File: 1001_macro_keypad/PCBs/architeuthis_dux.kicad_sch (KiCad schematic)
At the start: 32 parts, among them J1 ePaperModule, J2 RotaryModule_01, J3 RotaryModule_02, SW01 MX_SW, SW10 MX_SW, SW11 MX_SW, SW12 MX_SW, SW13 MX_SW, SW14 MX_SW, SW2 MX_SW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

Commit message: epaper 테스트
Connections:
- net +5V: no longer J1.1 (BUSY)
- net VSYS: now reaches U1.39 (VSYS)
- net VSYS: now also J1.1 (BUSY)
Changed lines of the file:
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@@
+    )
+  )
+  (global_label "VSYS" (shape input) (at 208.28 77.47 180) (fields_autoplaced)
+    (effects (font (size 1.27 1.27)) (justify right))
+    (property "Intersheetrefs" "${INTERSHEET_REFS}" (at 200.778 77.47 0)
+      (effects (font (size 1.27 1.27)) (justify right) hide)
     )
   )
@@
     (effects (font (size 1.27 1.27)) (justify left))
     (property "Intersheetrefs" "${INTERSHEET_REFS}" (at 99.6072 49.53 0)
+      (effects (font (size 1.27 1.27)) (justify left) hide)
+    )
+  )
+  (global_label "VSYS" (shape input) (at 151.13 44.45 0) (fields_autoplaced)
+    (effects (font (size 1.27 1.27)) (justify left))
+    (property "Intersheetrefs" "${INTERSHEET_REFS}" (at 158.632 44.45 0)
       (effects (font (size 1.27 1.27)) (justify left) hide)
     )
@@
         )
       )
-    )
-  )
-  (symbol (lib_id "power:+5V") (at 208.28 77.47 90) (unit 1)
-    (in_bom yes) (on_board yes) (dnp no) (fields_autoplaced)
-    (property "Reference" "#PWR02" (at 212.09 77.47 0)
-      (effects (font (size 1.27 1.27)) hide)
-    )
-    (property "Value" "+5V" (at 204.47 78.105 90)
-      (effects (font (size 1.27 1.27)) (justify left))
-    )
-    (property "Footprint" "" (at 208.28 77.47 0)
-      (effects (font (size 1.27 1.27)) hide)
-    )
-    (property "Datasheet" "" (at 208.28 77.47 0)
-      (effects (font (size 1.27 1.27)) hide)
-    )
-    (pin "1")
-    (instances
-      (project "architeuthis_dux"
-        (path "/4d2fbfb9-c67d-4ccb-bbaa-2d2f4be0cbd8"
-          (reference "#PWR02") (unit 1)
-        )
-      )

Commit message: 배선 변경 및 라이브러리 추가
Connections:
- net at J2.2 (KEY): no longer U1.25 (GPIO19)
- net at J2.3 (S2): no longer U1.24 (GPIO18)
- net at J2.4 (S1): no longer U1.22 (GPIO17)
- net at J3.2 (Pin_2): no longer U1.21 (GPIO16)
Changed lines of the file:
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@@
-    (stroke (width 0) (type default))
-  )
-  (wire (pts (xy 161.29 109.22) (xy 176.53 109.22))
     (stroke (width 0) (type default))
   )
@@
     (stroke (width 0) (type default))
   )
-  (wire (pts (xy 161.29 90.17) (xy 161.29 109.22))
-    (stroke (width 0) (type default))
-  )
   (wire (pts (xy 48.26 99.06) (xy 60.96 99.06))
     (stroke (width 0) (type default))
   )
-  (wire (pts (xy 151.13 80.01) (xy 167.64 80.01))
-    (stroke (width 0) (type default))
-  )
   (wire (pts (xy 115.57 90.17) (xy 115.57 114.3))
-    (stroke (width 0) (type default))
-  )
-  (wire (pts (xy 167.64 93.98) (xy 176.53 93.98))
-    (stroke (width 0) (type default))
-  )
-  (wire (pts (xy 167.64 80.01) (xy 167.64 93.98))
     (stroke (width 0) (type default))
   )
@@
     (stroke (width 0) (type default))
   )
-  (wire (pts (xy 163.83 87.63) (xy 163.83 99.06))
-    (stroke (width 0) (type default))
-  )
   (wire (pts (xy 151.13 74.93) (xy 191.77 74.93))
     (stroke (width 0) (type default))
   )
   (wire (pts (xy 53.34 96.52) (xy 38.1 96.52))
-    (stroke (width 0) (type default))
-  )
-  (wire (pts (xy 165.1 96.52) (xy 176.53 96.52))
     (stroke (width 0) (type default))
   )
@@
     (stroke (width 0) (type default))
   )
-  (wire (pts (xy 163.83 99.06) (xy 176.53 99.06))
-    (stroke (width 0) (type default))
-  )
   (wire (pts (xy 66.04 93.98) (xy 53.34 93.98))
-    (stroke (width 0) (type default))
-  )
-  (wire (pts (xy 151.13 82.55) (xy 165.1 82.55))
     (stroke (width 0) (type default))
   )
@@
     (stroke (width 0) (type default))
   )
-  (wire (pts (xy 151.13 90.17) (xy 161.29 90.17))
-    (stroke (width 0) (type default))
-  )
   (wire (pts (xy 189.23 77.47) (xy 151.13 77.47))
     (stroke (width 0) (type default))
   )
   (wire (pts (xy 81.28 66.04) (xy 91.44 66.04))
-    (stroke (width 0) (type default))
-  )
-  (wire (pts (xy 151.13 87.63) (xy 163.83 87.63))
     (stroke (width 0) (type default))
   )
@@
     (stroke (width 0) (type default))
   )
-  (wire (pts (xy 165.1 82.55) (xy 165.1 96.52))
-    (stroke (width 0) (type default))
-  )

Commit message: 설계 픽스 및 모델링 작업 시작
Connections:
- net at J1.3 (D/C): now also U1.25 (GPIO19); no longer U1.34 (GPIO28_ADC2)
- net at J1.4 (CS): now also U1.24 (GPIO18); no longer U1.26 (GPIO20)
- net at J1.5 (SCL): now also U1.26 (GPIO20); no longer U1.32 (GPIO27_ADC1)
- net at J1.6 (SDA): now also U1.21 (GPIO16); no longer U1.27 (GPIO21)
- net at J1.7 (GND): now also U1.22 (GPIO17); no longer U1.31 (GPIO26_ADC0)
- net at J1.8 (VCC): now also U1.27 (GPIO21); no longer U1.29 (GPIO22)
- net at J2.2 (KEY): now also U1.11 (GPIO8)
- net at J2.3 (S2): now also U1.12 (GPIO9)
- net at J2.4 (S1): now also U1.14 (GPIO10)
- net at J3.2 (Pin_2): now also U1.17 (GPIO13)
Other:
- moved on the sheet: J1
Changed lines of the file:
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@@
   (junction (at 81.28 49.53) (diameter 0) (color 0 0 0 0)
   )
-  (wire (pts (xy 199.39 87.63) (xy 208.28 87.63))
-    (stroke (width 0) (type default))
-  )
   (wire (pts (xy 45.72 111.76) (xy 45.72 125.73))
     (stroke (width 0) (type default))
   )
-  (wire (pts (xy 200.66 57.15) (xy 151.13 57.15))
+  (wire (pts (xy 171.45 77.47) (xy 171.45 64.77))
     (stroke (width 0) (type default))
   )
@@
     (stroke (width 0) (type default))
   )
+  (wire (pts (xy 151.13 90.17) (xy 168.91 90.17))
+    (stroke (width 0) (type default))
+  )
   (wire (pts (xy 38.1 111.76) (xy 45.72 111.76))
     (stroke (width 0) (type default))
   )
-  (wire (pts (xy 189.23 85.09) (xy 189.23 77.47))
-    (stroke (width 0) (type default))
-  )
-  (wire (pts (xy 208.28 95.25) (xy 194.31 95.25))
-    (stroke (width 0) (type default))
-  )
-  (wire (pts (xy 199.39 62.23) (xy 199.39 87.63))
-    (stroke (width 0) (type default))
-  )
-  (wire (pts (xy 113.03 111.76) (xy 113.03 87.63))
-    (stroke (width 0) (type default))
-  )
   (wire (pts (xy 48.26 49.53) (xy 64.77 49.53))
     (stroke (width 0) (type default))
   )
+  (wire (pts (xy 151.13 82.55) (xy 167.64 82.55))
+    (stroke (width 0) (type default))
+  )
+  (wire (pts (xy 115.57 90.17) (xy 101.6 90.17))
+    (stroke (width 0) (type default))
+  )
+  (wire (pts (xy 101.6 90.17) (xy 101.6 114.3))
+    (stroke (width 0) (type default))
+  )
   (wire (pts (xy 33.02 99.06) (xy 48.26 99.06))
     (stroke (width 0) (type default))
   )
-  (wire (pts (xy 176.53 111.76) (xy 113.03 111.76))
-    (stroke (width 0) (type default))
-  )
   (wire (pts (xy 64.77 66.04) (xy 81.28 66.04))
     (stroke (width 0) (type default))
   )
+  (wire (pts (xy 176.53 93.98) (xy 109.22 93.98))
+    (stroke (width 0) (type default))
+  )
   (wire (pts (xy 48.26 99.06) (xy 60.96 99.06))
     (stroke (width 0) (type default))
   )
-  (wire (pts (xy 115.57 90.17) (xy 115.57 114.3))
+  (wire (pts (xy 104.14 74.93) (xy 104.14 99.06))
     (stroke (width 0) (type default))
   )
@@
     (stroke (width 0) (type default))
   )
-  (wire (pts (xy 208.28 92.71) (xy 196.85 92.71))
-    (stroke (width 0) (type default))
-  )
-  (wire (pts (xy 208.28 82.55) (xy 200.66 82.55))
-    (stroke (width 0) (type default))
-  )
-  (wire (pts (xy 200.66 82.55) (xy 200.66 57.15))
-    (stroke (width 0) (type default))
-  )
-  (wire (pts (xy 113.03 87.63) (xy 115.57 87.63))
-    (stroke (width 0) (type default))
-  )
   (wire (pts (xy 38.1 111.76) (xy 38.1 115.57))
     (stroke (width 0) (type default))
   )
-  (wire (pts (xy 151.13 62.23) (xy 199.39 62.23))
-    (stroke (width 0) (type default))
-  )
   (wire (pts (xy 53.34 111.76) (xy 53.34 115.57))
     (stroke (width 0) (type default))
   )
-  (wire (pts (xy 151.13 74.93) (xy 191.77 74.93))
+  (wire (pts (xy 165.1 59.69) (xy 177.8 59.69))
+    (stroke (width 0) (type default))
+  )
+  (wire (pts (xy 173.99 69.85) (xy 177.8 69.85))
+    (stroke (width 0) (type default))
+  )
+  (wire (pts (xy 168.91 67.31) (xy 177.8 67.31))
+    (stroke (width 0) (type default))
+  )
+  (wire (pts (xy 176.53 114.3) (xy 101.6 114.3))
     (stroke (width 0) (type default))
   )
@@
     (stroke (width 0) (type default))
   )
+  (wire (pts (xy 151.13 80.01) (xy 165.1 80.01))
+    (stroke (width 0) (type default))
+  )
   (wire (pts (xy 38.1 93.98) (xy 38.1 96.52))
     (stroke (width 0) (type default))
   )
+  (wire (pts (xy 106.68 96.52) (xy 106.68 69.85))
+    (stroke (width 0) (type default))
+  )
+  (wire (pts (xy 110.49 87.63) (xy 115.57 87.63))
+    (stroke (width 0) (type default))
+  )
   (wire (pts (xy 66.04 125.73) (xy 66.04 93.98))
     (stroke (width 0) (type default))
@@
     (stroke (width 0) (type default))
   )
+  (wire (pts (xy 109.22 67.31) (xy 109.22 93.98))
+    (stroke (width 0) (type default))
+  )
   (wire (pts (xy 53.34 111.76) (xy 53.34 96.52))
     (stroke (width 0) (type default))
   )
+  (wire (pts (xy 167.64 82.55) (xy 167.64 62.23))
+    (stroke (width 0) (type default))
+  )
+  (wire (pts (xy 106.68 69.85) (xy 115.57 69.85))
+    (stroke (width 0) (type default))
+  )
   (wire (pts (xy 66.04 93.98) (xy 53.34 93.98))
     (stroke (width 0) (type default))
@@
     (stroke (width 0) (type default))
   )
-  (wire (pts (xy 115.57 114.3) (xy 176.53 114.3))
-    (stroke (width 0) (type default))
-  )
-  (wire (pts (xy 191.77 74.93) (xy 191.77 90.17))
+  (wire (pts (xy 113.03 82.55) (xy 113.03 109.22))
+    (stroke (width 0) (type default))
+  )
+  (wire (pts (xy 104.14 74.93) (xy 115.57 74.93))
+    (stroke (width 0) (type default))
+  )
+  (wire (pts (xy 151.13 74.93) (xy 177.8 74.93))
+    (stroke (width 0) (type default))
+  )
+  (wire (pts (xy 151.13 87.63) (xy 173.99 87.63))
+    (stroke (width 0) (type default))
+  )
+  (wire (pts (xy 168.91 90.17) (xy 168.91 67.31))
     (stroke (width 0) (type default))
   )
@@
     (stroke (width 0) (type default))
   )
-  (wire (pts (xy 194.31 69.85) (xy 151.13 69.85))
-    (stroke (width 0) (type default))
-  )
-  (wire (pts (xy 194.31 95.25) (xy 194.31 69.85))
+  (wire (pts (xy 176.53 109.22) (xy 113.03 109.22))
     (stroke (width 0) (type default))
   )
@@
     (stroke (width 0) (type default))
   )
-  (wire (pts (xy 208.28 85.09) (xy 189.23 85.09))
-    (stroke (width 0) (type default))
-  )
   (wire (pts (xy 86.36 93.98) (xy 86.36 78.74))
     (stroke (width 0) (type default))
   )
-  (wire (pts (xy 191.77 90.17) (xy 208.28 90.17))
-    (stroke (width 0) (type default))
-  )
-  (wire (pts (xy 196.85 92.71) (xy 196.85 64.77))
+  (wire (pts (xy 109.22 67.31) (xy 115.57 67.31))
+    (stroke (width 0) (type default))
+  )
+  (wire (pts (xy 113.03 82.55) (xy 115.57 82.55))
     (stroke (width 0) (type default))
   )
@@
     (stroke (width 0) (type default))
   )
+  (wire (pts (xy 165.1 80.01) (xy 165.1 59.69))
+    (stroke (width 0) (type default))
+  )
+  (wire (pts (xy 173.99 87.63) (xy 173.99 69.85))
+    (stroke (width 0) (type default))
+  )
   (wire (pts (xy 48.26 81.28) (xy 64.77 81.28))
     (stroke (width 0) (type default))
@@
     (stroke (width 0) (type default))
   )
-  (wire (pts (xy 196.85 64.77) (xy 151.13 64.77))
-    (stroke (width 0) (type default))
-  )
-  (wire (pts (xy 189.23 77.47) (xy 151.13 77.47))
+  (wire (pts (xy 176.53 111.76) (xy 110.49 111.76))
+    (stroke (width 0) (type default))
+  )
+  (wire (pts (xy 167.64 62.23) (xy 177.8 62.23))
+    (stroke (width 0) (type default))
+  )
+  (wire (pts (xy 171.45 64.77) (xy 177.8 64.77))
+    (stroke (width 0) (type default))
+  )
+  (wire (pts (xy 177.8 74.93) (xy 177.8 72.39))
     (stroke (width 0) (type default))
   )
@@
     (stroke (width 0) (type default))
   )
+  (wire (pts (xy 110.49 111.76) (xy 110.49 87.63))
+    (stroke (width 0) (type default))
+  )
   (wire (pts (xy 33.02 66.04) (xy 48.26 66.04))
     (stroke (width 0) (type default))
   )
   (wire (pts (xy 38.1 78.74) (xy 38.1 93.98))
+    (stroke (width 0) (type default))
+  )
+  (wire (pts (xy 176.53 99.06) (xy 104.14 99.06))
+    (stroke (width 0) (type default))
+  )
+  (wire (pts (xy 176.53 96.52) (xy 106.68 96.52))
+    (stroke (width 0) (type default))
+  )
+  (wire (pts (xy 151.13 77.47) (xy 171.45 77.47))
     (stroke (width 0) (type default))
   )
@@
     )
   )
-  (global_label "VSYS" (shape input) (at 208.28 77.47 180) (fields_autoplaced)
-    (effects (font (size 1.27 1.27)) (justify right))
-    (property "Intersheetrefs" "${INTERSHEET_REFS}" (at 200.778 77.47 0)
+  (global_label "VSYS" (shape input) (at 177.8 54.61 180) (fields_autoplaced)
+    (effects (font (size 1.27 1.27)) (justify right))
+    (property "Intersheetrefs" "${INTERSHEET_REFS}" (at 170.298 54.61 0)
       (effects (font (size 1.27 1.27)) (justify right) hide)
     )
@@
     )
   )
-  (symbol (lib_id "Connector_Generic:Conn_01x08") (at 213.36 85.09 0) (unit 1)
-    (in_bom yes) (on_board yes) (dnp no) (fields_autoplaced)
-    (property "Reference" "J1" (at 215.9 85.725 0)
+  (symbol (lib_id "Connector_Generic:Conn_01x08") (at 182.88 62.23 0) (unit 1)
+    (in_bom yes) (on_board yes) (dnp no) (fields_autoplaced)
+    (property "Reference" "J1" (at 185.42 62.865 0)
       (effects (font (size 1.27 1.27)) (justify left))
     )
-    (property "Value" "ePaperModule" (at 215.9 88.265 0)
+    (property "Value" "ePaperModule" (at 185.42 65.405 0)
       (effects (font (size 1.27 1.27)) (justify left))
     )
-    (property "Footprint" "Connector_PinHeader_2.54mm:PinHeader_2x04_P2.54mm_Vertical" (at 213.36 85.09 0)
-      (effects (font (size 1.27 1.27)) hide)
-    )
-    (property "Datasheet" "~" (at 213.36 85.09 0)
+    (property "Footprint" "Connector_PinHeader_2.54mm:PinHeader_2x04_P2.54mm_Vertical" (at 182.88 62.23 0)
+      (effects (font (size 1.27 1.27)) hide)
+    )
+    (property "Datasheet" "~" (at 182.88 62.23 0)
       (effects (font (size 1.27 1.27)) hide)
     )
@@
     )
   )
-  (symbol (lib_id "power:GND") (at 208.28 80.01 270) (unit 1)
-    (in_bom yes) (on_board yes) (dnp no) (fields_autoplaced)
-    (property "Reference" "#PWR014" (at 201.93 80.01 0)
-      (effects (font (size 1.27 1.27)) hide)
-    )
-    (property "Value" "GND" (at 204.47 80.645 90)
-      (effects (font (size 1.27 1.27)) (justify right))
-    )
-    (property "Footprint" "" (at 208.28 80.01 0)
-      (effects (font (size 1.27 1.27)) hide)
-    )
-    (property "Datasheet" "" (at 208.28 80.01 0)
-      (effects (font (size 1.27 1.27)) hide)
-    )
+  (symbol (lib_id "power:GND") (at 177.8 57.15 270) (unit 1)
+    (in_bom yes) (on_board yes) (dnp no) (fields_autoplaced)
+    (property "Reference" "#PWR014" (at 171.45 57.15 0)
+      (effects (font (size 1.27 1.27)) hide)
+    )
+    (property "Value" "GND" (at 173.99 57.785 90)
+      (effects (font (size 1.27 1.27)) (justify right))
+    )
+    (property "Footprint" "" (at 177.8 57.15 0)
+      (effects (font (size 1.27 1.27)) hide)
+    )
+    (property "Datasheet" "" (at 177.8 57.15 0)
+      (effects (font (size 1.27 1.27)) hide)
+    )

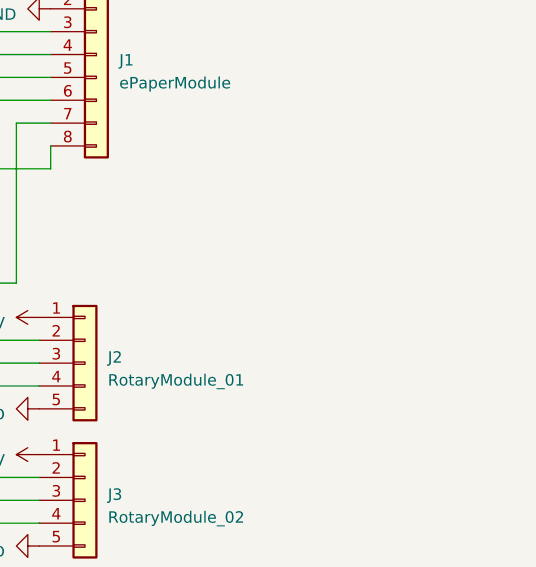
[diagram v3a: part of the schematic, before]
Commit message: 레퍼런스 리소스 추가 및 하부 케이스 모델링 시작
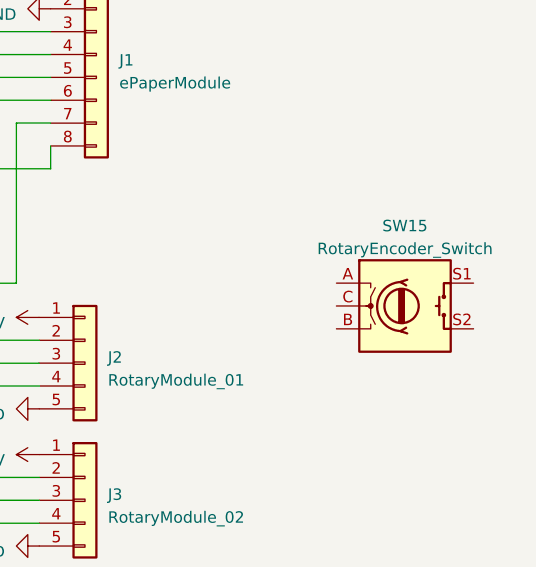
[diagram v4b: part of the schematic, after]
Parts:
- added SW15: RotaryEncoder_Switch, symbol Device:RotaryEncoder_Switch
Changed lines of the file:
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@@
+    )
+  )
+  (symbol (lib_id "Device:RotaryEncoder_Switch") (at 217.17 90.17 0) (unit 1)
+    (in_bom yes) (on_board yes) (dnp no) (fields_autoplaced)
+    (property "Reference" "SW15" (at 217.17 81.28 0)
+      (effects (font (size 1.27 1.27)))
+    )
+    (property "Value" "RotaryEncoder_Switch" (at 217.17 83.82 0)
+      (effects (font (size 1.27 1.27)))
+    )
+    (property "Footprint" "" (at 213.36 86.106 0)
+      (effects (font (size 1.27 1.27)) hide)
+    )
+    (property "Datasheet" "~" (at 217.17 83.566 0)
+      (effects (font (size 1.27 1.27)) hide)
+    )
+    (pin "A")
+    (pin "B")
+    (pin "C")
+    (pin "S1")
+    (pin "S2")
+    (instances
+      (project "architeuthis_dux"
+        (path "/4d2fbfb9-c67d-4ccb-bbaa-2d2f4be0cbd8"
+          (reference "SW15") (unit 1)
+        )
+      )
     )
   )
